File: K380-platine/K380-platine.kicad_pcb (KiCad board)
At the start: 2 copper layers, 98 x 38 mm, 32 parts, among them J1 JST-PH 2, J2 Conn_01x23, J3 MicroMod-M.2E, J4 USB_C_Receptacle_USB2.0, J5 Conn_ARM_JTAG_SWD_10, Q1 PMost Enc FET -20V, Q2 Q_NMOS_DGS, SW1 EG1215AA, SW2 SW_Push, SW3 SW_Push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

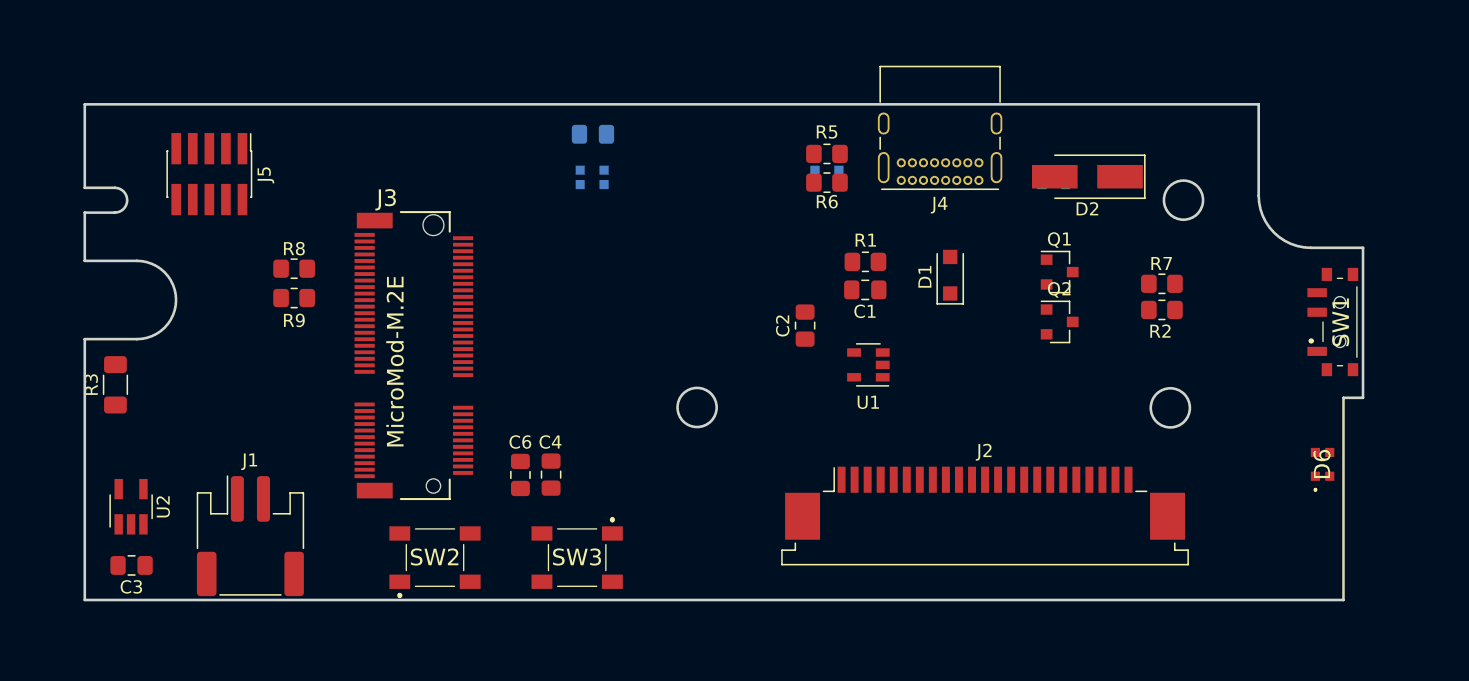
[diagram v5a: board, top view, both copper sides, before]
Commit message: Small layout changes to improve routing
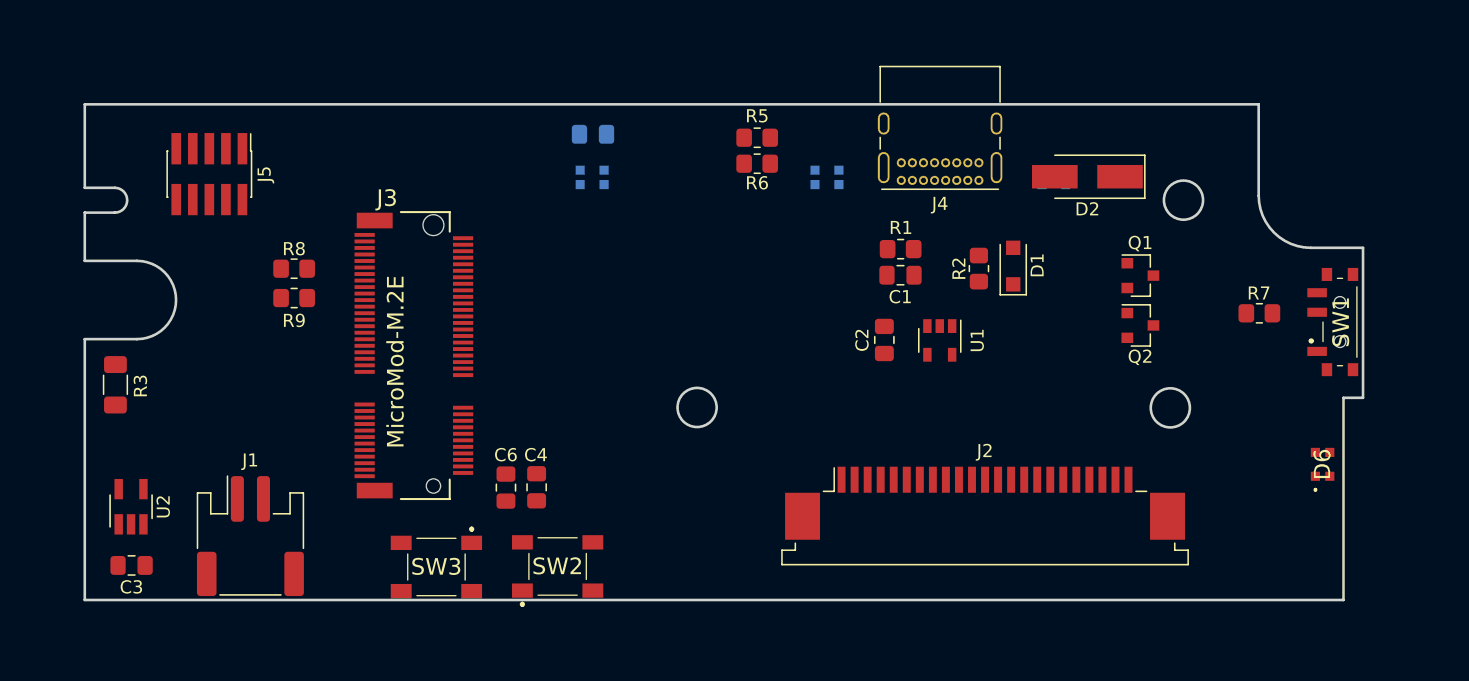
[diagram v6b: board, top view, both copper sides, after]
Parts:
- moved R2 14.4 mm to (144.2, 75.0), turned to 90 degrees
- moved SW3 10.8 mm to (102.7, 97.9)
- moved SW2 9.42 mm to (112.0, 97.8)
- moved R7 7.80 mm to (165.8, 78.4)
- moved Q1 6.20 mm to (156.6, 75.5)
- moved Q2 6.20 mm to (156.6, 79.3)
- moved C2 6.17 mm to (137.0, 80.5)
- moved U1 5.79 mm to (141.2, 80.5), turned to 270 degrees
- moved R6 5.54 mm to (127.2, 67.0)
- moved R5 5.49 mm to (127.2, 65.0)
- moved D1 4.88 mm to (146.9, 74.8)
- moved C1 2.93 mm to (138.2, 75.5)
- moved R1 2.87 mm to (138.2, 73.5)
- moved C4 1.47 mm to (110.3, 91.8)
- moved C6 1.47 mm to (108.0, 91.8)
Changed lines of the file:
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@@
   )
   (module Resistor_SMD:R_0805_2012Metric_Pad1.20x1.40mm_HandSolder (layer F.Cu)
-    (at 158.28 76.16)
+    (at 165.75 78.42)
     (descr "Resistor SMD 0805 (2012 Metric), square (rectangular) end terminal, IPC_7351 nominal with elongated pad for handsoldering. (Body size source: IPC-SM-782 page 72, https://www.pcb-3d.com/wordpress/wp-content/uploads/ipc-sm-782a_amendment_1_and_2.pdf), generated with kicad-footprint-generator")
     (tags "resistor handsolder")
@@
   )
   (module Resistor_SMD:R_0805_2012Metric_Pad1.20x1.40mm_HandSolder (layer F.Cu)
-    (at 132.6 68.4)
+    (at 127.25 66.95)
     (descr "Resistor SMD 0805 (2012 Metric), square (rectangular) end terminal, IPC_7351 nominal with elongated pad for handsoldering. (Body size source: IPC-SM-782 page 72, https://www.pcb-3d.com/wordpress/wp-content/uploads/ipc-sm-782a_amendment_1_and_2.pdf), generated with kicad-footprint-generator")
     (tags "resistor handsolder")
@@
   )
   (module Resistor_SMD:R_0805_2012Metric_Pad1.20x1.40mm_HandSolder (layer F.Cu)
-    (at 132.6 66.2)
+    (at 127.25 64.96)
     (descr "Resistor SMD 0805 (2012 Metric), square (rectangular) end terminal, IPC_7351 nominal with elongated pad for handsoldering. (Body size source: IPC-SM-782 page 72, https://www.pcb-3d.com/wordpress/wp-content/uploads/ipc-sm-782a_amendment_1_and_2.pdf), generated with kicad-footprint-generator")
     (tags "resistor handsolder")
@@
   )
   (module Resistor_SMD:R_0805_2012Metric_Pad1.20x1.40mm_HandSolder (layer F.Cu)
-    (at 158.28 78.16)
+    (at 144.25 74.99 90)
     (descr "Resistor SMD 0805 (2012 Metric), square (rectangular) end terminal, IPC_7351 nominal with elongated pad for handsoldering. (Body size source: IPC-SM-782 page 72, https://www.pcb-3d.com/wordpress/wp-content/uploads/ipc-sm-782a_amendment_1_and_2.pdf), generated with kicad-footprint-generator")
     (tags "resistor handsolder")
     (attr smd)
-    (fp_text reference R2 (at -0.11 1.67) (layer F.SilkS)
-      (effects (font (size 1 1) (thickness 0.15)))
-    )
-    (fp_text value 100K (at 0 1.65) (layer F.Fab)
-      (effects (font (size 1 1) (thickness 0.15)))
-    )
-    (fp_text user %R (at 0 0) (layer F.Fab)
+    (fp_text reference R2 (at -0.01 -1.5 90) (layer F.SilkS)
+      (effects (font (size 1 1) (thickness 0.15)))
+    )
+    (fp_text value 100K (at 0 1.65 90) (layer F.Fab)
+      (effects (font (size 1 1) (thickness 0.15)))
+    )
+    (fp_text user %R (at 0 0 90) (layer F.Fab)
       (effects (font (size 0.5 0.5) (thickness 0.08)))
     )
@@
     (fp_line (start 1.85 -0.95) (end 1.85 0.95) (layer F.CrtYd) (width 0.05))
     (fp_line (start 1.85 0.95) (end -1.85 0.95) (layer F.CrtYd) (width 0.05))
-    (pad 2 smd roundrect (at 1 0) (size 1.2 1.4) (layers F.Cu F.Paste F.Mask) (roundrect_rratio 0.208333)
+    (pad 2 smd roundrect (at 1 0 90) (size 1.2 1.4) (layers F.Cu F.Paste F.Mask) (roundrect_rratio 0.208333)
       (net 19 "Net-(C1-Pad1)"))
-    (pad 1 smd roundrect (at -1 0) (size 1.2 1.4) (layers F.Cu F.Paste F.Mask) (roundrect_rratio 0.208333)
+    (pad 1 smd roundrect (at -1 0 90) (size 1.2 1.4) (layers F.Cu F.Paste F.Mask) (roundrect_rratio 0.208333)
       (net 62 "Net-(R2-Pad1)"))
     (model ${KISYS3DMOD}/Resistor_SMD.3dshapes/R_0805_2012Metric.wrl
@@
   )
   (module Resistor_SMD:R_0805_2012Metric_Pad1.20x1.40mm_HandSolder (layer F.Cu)
-    (at 135.55 74.475 180)
+    (at 138.25 73.5 180)
     (descr "Resistor SMD 0805 (2012 Metric), square (rectangular) end terminal, IPC_7351 nominal with elongated pad for handsoldering. (Body size source: IPC-SM-782 page 72, https://www.pcb-3d.com/wordpress/wp-content/uploads/ipc-sm-782a_amendment_1_and_2.pdf), generated with kicad-footprint-generator")
     (tags "resistor handsolder")
@@
   )
   (module Capacitor_SMD:C_0805_2012Metric_Pad1.18x1.45mm_HandSolder (layer F.Cu)
-    (at 109.1 90.8125 270)
+    (at 107.99 91.7825 270)
     (descr "Capacitor SMD 0805 (2012 Metric), square (rectangular) end terminal, IPC_7351 nominal with elongated pad for handsoldering. (Body size source: IPC-SM-782 page 76, https://www.pcb-3d.com/wordpress/wp-content/uploads/ipc-sm-782a_amendment_1_and_2.pdf, https://docs.google.com/spreadsheets/d/1BsfQQcO9C6DZCsRaXUlFlo91Tg2WpOkGARC1WS5S8t0/edit?usp=sharing), generated with kicad-footprint-generator")
     (tags "capacitor handsolder")
@@
   )
   (module Capacitor_SMD:C_0805_2012Metric_Pad1.18x1.45mm_HandSolder (layer F.Cu)
-    (at 111.45 90.7875 270)
+    (at 110.34 91.7575 270)
     (descr "Capacitor SMD 0805 (2012 Metric), square (rectangular) end terminal, IPC_7351 nominal with elongated pad for handsoldering. (Body size source: IPC-SM-782 page 76, https://www.pcb-3d.com/wordpress/wp-content/uploads/ipc-sm-782a_amendment_1_and_2.pdf, https://docs.google.com/spreadsheets/d/1BsfQQcO9C6DZCsRaXUlFlo91Tg2WpOkGARC1WS5S8t0/edit?usp=sharing), generated with kicad-footprint-generator")
     (tags "capacitor handsolder")
@@
   )
   (module Capacitor_SMD:C_0805_2012Metric_Pad1.18x1.45mm_HandSolder (layer F.Cu)
-    (at 130.925 79.3625 90)
+    (at 137 80.4625 90)
     (descr "Capacitor SMD 0805 (2012 Metric), square (rectangular) end terminal, IPC_7351 nominal with elongated pad for handsoldering. (Body size source: IPC-SM-782 page 76, https://www.pcb-3d.com/wordpress/wp-content/uploads/ipc-sm-782a_amendment_1_and_2.pdf, https://docs.google.com/spreadsheets/d/1BsfQQcO9C6DZCsRaXUlFlo91Tg2WpOkGARC1WS5S8t0/edit?usp=sharing), generated with kicad-footprint-generator")
     (tags "capacitor handsolder")
@@
   )
   (module Capacitor_SMD:C_0805_2012Metric_Pad1.18x1.45mm_HandSolder (layer F.Cu)
-    (at 135.5375 76.625 180)
+    (at 138.2375 75.5 180)
     (descr "Capacitor SMD 0805 (2012 Metric), square (rectangular) end terminal, IPC_7351 nominal with elongated pad for handsoldering. (Body size source: IPC-SM-782 page 76, https://www.pcb-3d.com/wordpress/wp-content/uploads/ipc-sm-782a_amendment_1_and_2.pdf, https://docs.google.com/spreadsheets/d/1BsfQQcO9C6DZCsRaXUlFlo91Tg2WpOkGARC1WS5S8t0/edit?usp=sharing), generated with kicad-footprint-generator")
     (tags "capacitor handsolder")
@@
   )
   (module LibraryLoader:MJTP1140AAUTR (layer F.Cu)
-    (at 113.45 97.15 180)
+    (at 102.66 97.87 180)
     (descr MJTP1140AAUTR-3)
     (tags Switch)
@@
   )
   (module LibraryLoader:MJTP1140AAUTR (layer F.Cu)
-    (at 102.55 97.15)
+    (at 111.95 97.83)
     (descr MJTP1140AAUTR-3)
     (tags Switch)
@@
     (tags "resistor handsolder")
     (attr smd)
-    (fp_text reference R3 (at 0 -1.82 90) (layer F.SilkS)
-      (effects (font (size 1 1) (thickness 0.15)))
-    )
-    (fp_text value RProg (at 0 1.82 90) (layer F.Fab)
+    (fp_text reference R3 (at -0.1 1.95 90) (layer F.SilkS)
+      (effects (font (size 1 1) (thickness 0.15)))
+    )
+    (fp_text value RProg (at -0.1 -1.8 90) (layer F.Fab)
       (effects (font (size 1 1) (thickness 0.15)))
     )
@@
   )
   (module Package_TO_SOT_SMD:SOT-23 (layer F.Cu)
-    (at 150.44 79.08)
+    (at 156.63 79.35)
     (descr "SOT-23, Standard")
     (tags SOT-23)
     (attr smd)
-    (fp_text reference Q2 (at 0 -2.5) (layer F.SilkS)
+    (fp_text reference Q2 (at 0 2.4) (layer F.SilkS)
       (effects (font (size 1 1) (thickness 0.15)))
     )
@@
   )
   (module Diode_SMD:D_SOD-123F (layer F.Cu)
-    (at 142.05 75.5 90)
+    (at 146.88 74.8 90)
     (descr D_SOD-123F)
     (tags D_SOD-123F)
     (attr smd)
-    (fp_text reference D1 (at -0.127 -1.905 90) (layer F.SilkS)
+    (fp_text reference D1 (at 0.05 1.87 90) (layer F.SilkS)
       (effects (font (size 1 1) (thickness 0.15)))
     )
@@
   )
   (module Package_TO_SOT_SMD:SOT-23-5 (layer F.Cu)
-    (at 135.775 82.375 180)
+    (at 141.25 80.5 270)
     (descr "5-pin SOT23 package")
     (tags SOT-23-5)
     (attr smd)
-    (fp_text reference U1 (at 0 -2.9) (layer F.SilkS)
-      (effects (font (size 1 1) (thickness 0.15)))
-    )
-    (fp_text value XC6220B331MR (at 0 2.9) (layer F.Fab)
+    (fp_text reference U1 (at 0 -2.9 90) (layer F.SilkS)
+      (effects (font (size 1 1) (thickness 0.15)))
+    )
+    (fp_text value XC6220B331MR (at 0 2.9 90) (layer F.Fab)
       (effects (font (size 1 1) (thickness 0.15)))
     )
@@
     (fp_line (start 0.9 -1.61) (end -1.55 -1.61) (layer F.SilkS) (width 0.12))
     (fp_line (start -0.9 1.61) (end 0.9 1.61) (layer F.SilkS) (width 0.12))
-    (fp_text user %R (at 0 0 90) (layer F.Fab)
+    (fp_text user %R (at 0 0) (layer F.Fab)
       (effects (font (size 0.5 0.5) (thickness 0.075)))
     )
-    (pad 5 smd rect (at 1.1 -0.95 180) (size 1.06 0.65) (layers F.Cu F.Paste F.Mask)
+    (pad 5 smd rect (at 1.1 -0.95 270) (size 1.06 0.65) (layers F.Cu F.Paste F.Mask)
       (net 20 V3.3))
-    (pad 4 smd rect (at 1.1 0.95 180) (size 1.06 0.65) (layers F.Cu F.Paste F.Mask)
+    (pad 4 smd rect (at 1.1 0.95 270) (size 1.06 0.65) (layers F.Cu F.Paste F.Mask)
       (net 2 "Net-(U1-Pad4)"))
-    (pad 3 smd rect (at -1.1 0.95 180) (size 1.06 0.65) (layers F.Cu F.Paste F.Mask)
+    (pad 3 smd rect (at -1.1 0.95 270) (size 1.06 0.65) (layers F.Cu F.Paste F.Mask)
       (net 62 "Net-(R2-Pad1)"))
-    (pad 2 smd rect (at -1.1 0 180) (size 1.06 0.65) (layers F.Cu F.Paste F.Mask)
-      (net 18 GND))
-    (pad 1 smd rect (at -1.1 -0.95 180) (size 1.06 0.65) (layers F.Cu F.Paste F.Mask)
+    (pad 2 smd rect (at -1.1 0 270) (size 1.06 0.65) (layers F.Cu F.Paste F.Mask)
+      (net 18 GND))
+    (pad 1 smd rect (at -1.1 -0.95 270) (size 1.06 0.65) (layers F.Cu F.Paste F.Mask)
       (net 19 "Net-(C1-Pad1)"))
     (model ${KISYS3DMOD}/Package_TO_SOT_SMD.3dshapes/SOT-23-5.wrl
@@
   )
   (module Package_TO_SOT_SMD:SOT-23 (layer F.Cu)
-    (at 150.44 75.26)
+    (at 156.63 75.53)
     (descr "SOT-23, Standard")
     (tags SOT-23)

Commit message: Finished routing
- GND is zone fill in bottom
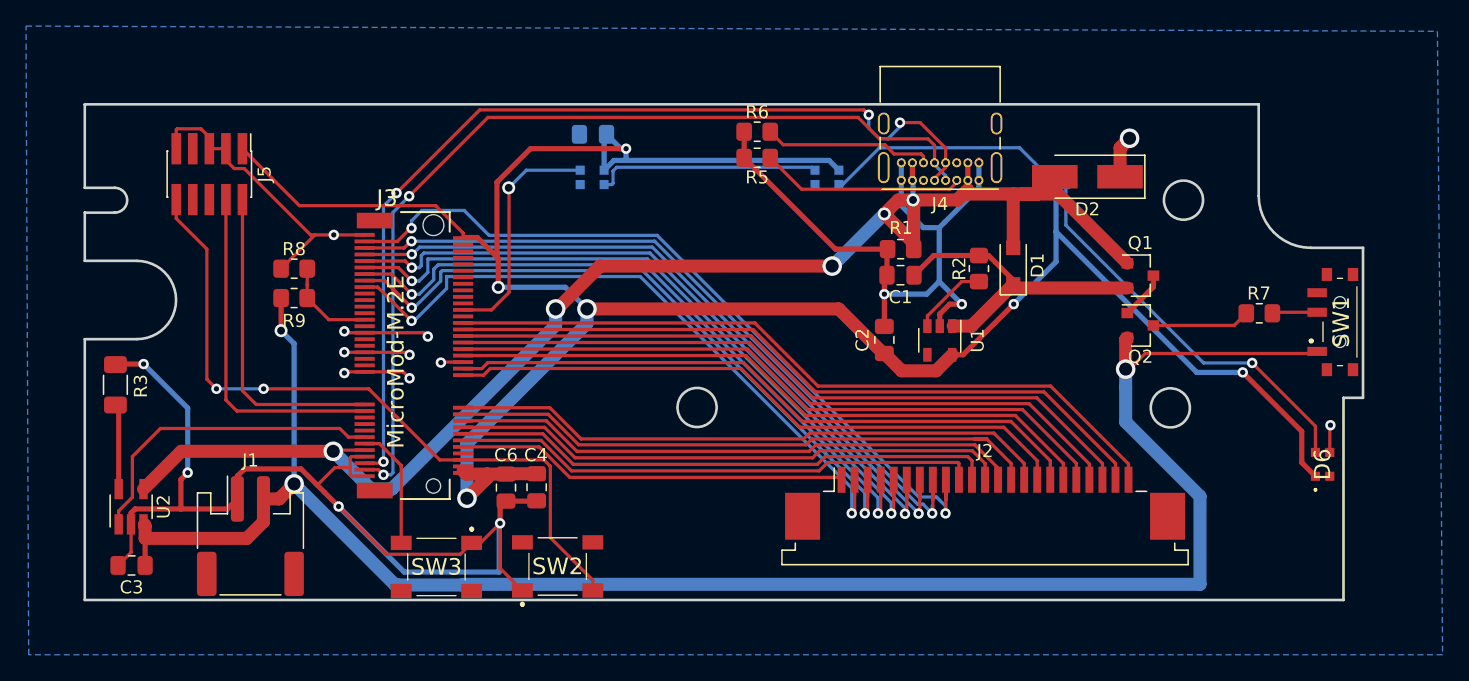
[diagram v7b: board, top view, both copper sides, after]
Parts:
- moved R6 2.45 mm to (127.2, 64.5)
- moved R5 1.54 mm to (127.2, 66.5)
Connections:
- J3 pad 59: ROW8 -> ROW1
- J3 pad 61: ROW7 -> ROW2
- J3 pad 63: ROW6 -> ROW3
- J3 pad 65: ROW5 -> ROW4
- J3 pad 67: ROW4 -> ROW5
- J3 pad 69: ROW3 -> ROW6
- J3 pad 71: ROW2 -> ROW7
- J3 pad 73: ROW1 -> ROW8
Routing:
- net GND: track 0.00 -> 186.1 mm, vias 0 -> 16
- net V3.3: track 0.00 -> 182.3 mm, vias 0 -> 6
- net VBAT: track 0.00 -> 156.8 mm, vias 0 -> 3
- net VUSB: track 0.00 -> 132.0 mm, vias 0 -> 5
- net D-: track 0.00 -> 73.3 mm, vias 0 -> 4
- net D+: track 0.00 -> 70.8 mm, vias 0 -> 2
- net ROW8: track 0.00 -> 60.2 mm, vias 0 -> 2
- net ROW7: track 0.00 -> 57.1 mm, vias 0 -> 2
- net COL15: track 0.00 -> 56.7 mm
- net COL14: track 0.00 -> 55.5 mm
- net ROW6: track 0.00 -> 55.3 mm, vias 0 -> 2
- net ROW5: track 0.00 -> 55.3 mm, vias 0 -> 2
- net ROW4: track 0.00 -> 54.8 mm, vias 0 -> 2
- net RESET: track 0.00 -> 54.7 mm, vias 0 -> 2
- net COL13: track 0.00 -> 54.3 mm
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- added copper zone on B.Cu, net GND
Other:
- net class Power added: clearance 0.2, trace_width 0.5, via_dia 1, via_drill 0.6

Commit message: Simplified tracks
as GND got to be the bottom layer, a few tracks were able be routed
differently, simplifying the layout and increasing the connection
between larger sections of GND.

Also on a few components connection to GND was given the same track
width as the power delivering lines connected to them.
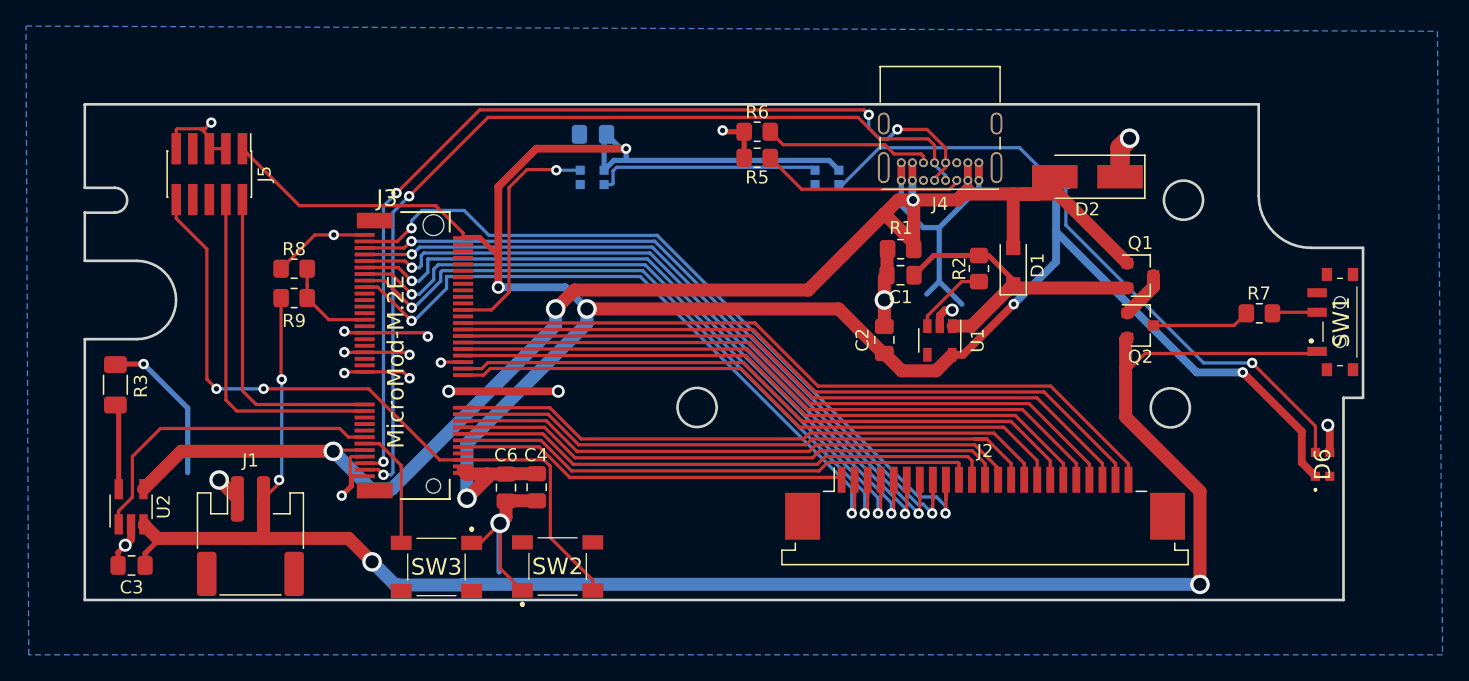
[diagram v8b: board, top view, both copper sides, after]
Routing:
- net GND: track 186.1 -> 122.5 mm, vias 16 -> 21
- net VBAT: track 156.8 -> 143.0 mm, vias 3 -> 4
- net D-: track 73.3 -> 74.6 mm
- net VUSB: vias 5 -> 3
